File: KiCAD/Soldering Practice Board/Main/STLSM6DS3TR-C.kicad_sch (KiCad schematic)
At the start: 1 part, among them U3 LSM6DS3

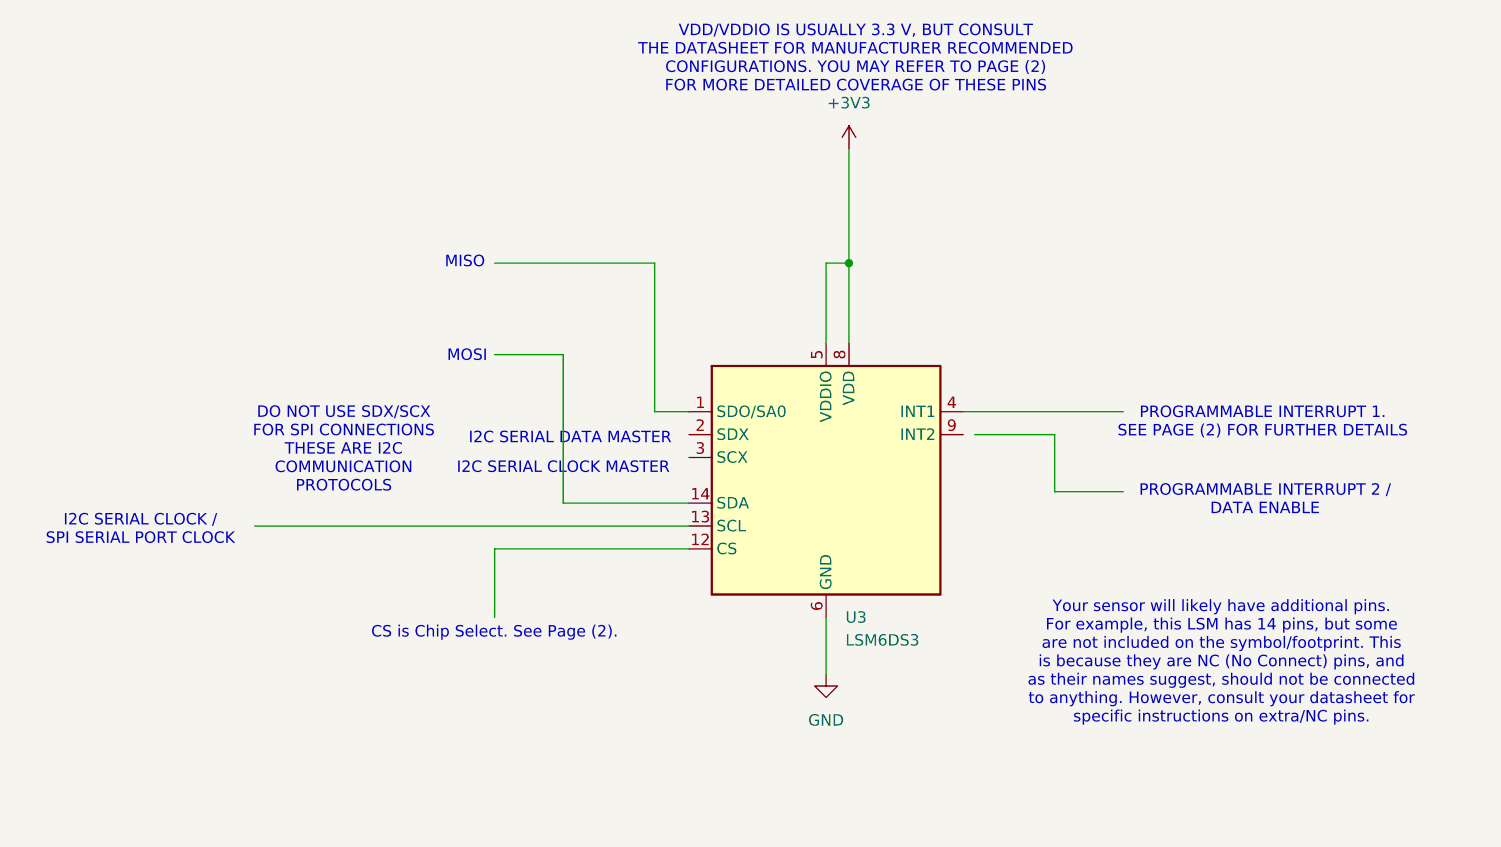
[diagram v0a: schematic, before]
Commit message: Make LIS3 labels more concise
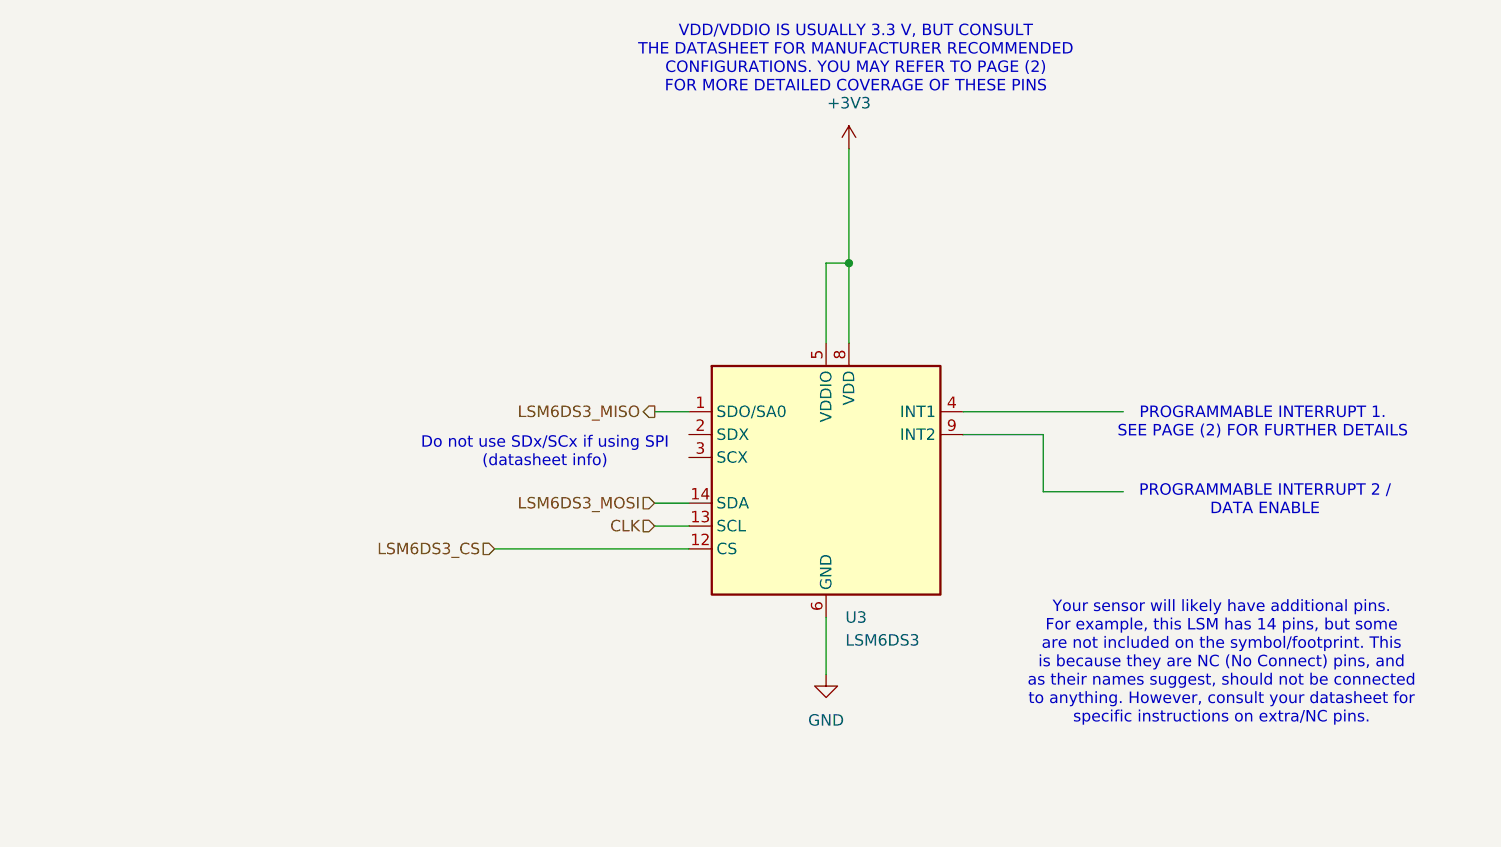
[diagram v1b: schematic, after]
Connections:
- net LSM6DS3_MISO: now reaches U3.1 (SDO/SA0)
- net LSM6DS3_CS: now reaches U3.12 (CS)
- net CLK: now reaches U3.13 (SCL)
- net LSM6DS3_MOSI: now reaches U3.14 (SDA)
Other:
- note added: "Do not use SDx/SCx if using SPI (datasheet info)"
- note removed: "CS is Chip Select. See Page (2)."
- note removed: "DO NOT USE SDX/SCX FOR SPI CONNECTIONS THESE ARE I2C COMMUNICATION PROTOCOLS"
- note removed: "I2C SERIAL CLOCK / SPI SERIAL PORT CLOCK"
- note removed: "I2C SERIAL CLOCK MASTER"
- note removed: "I2C SERIAL DATA MASTER"
- note removed: "MISO"
- note removed: "MOSI"
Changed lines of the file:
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@@
 	(generator_version "9.0")
 	(paper "A4")
-	(text "DO NOT USE SDX/SCX\nFOR SPI CONNECTIONS\nTHESE ARE I2C\nCOMMUNICATION\nPROTOCOLS"
-		(exclude_from_sim no)
-		(at 91.186 97.028 0)
+	(text "Do not use SDx/SCx if using SPI \n(datasheet info)"
+		(exclude_from_sim no)
+		(at 113.538 97.282 0)
 		(effects
 			(font
@@
 		)
 	)
-	(text "MOSI"
-		(exclude_from_sim no)
-		(at 104.902 86.614 0)
-		(effects
-			(font
-				(size 1.27 1.27)
-			)
-		)
-	)
-	(text "I2C SERIAL DATA MASTER"
-		(exclude_from_sim no)
-		(at 116.332 95.758 0)
-		(effects
-			(font
-				(size 1.27 1.27)
-			)
-		)
-	)
 	(text "VDD/VDDIO IS USUALLY 3.3 V, BUT CONSULT\nTHE DATASHEET FOR MANUFACTURER RECOMMENDED\nCONFIGURATIONS. YOU MAY REFER TO PAGE (2)\nFOR MORE DETAILED COVERAGE OF THESE PINS"
 		(exclude_from_sim no)
@@
 		)
 	)
-	(text "MISO"
-		(exclude_from_sim no)
-		(at 104.648 76.2 0)
-		(effects
-			(font
-				(size 1.27 1.27)
-			)
-		)
-	)
 	(text "Your sensor will likely have additional pins.\nFor example, this LSM has 14 pins, but some\nare not included on the symbol/footprint. This\nis because they are NC (No Connect) pins, and \nas their names suggest, should not be connected\nto anything. However, consult your datasheet for\nspecific instructions on extra/NC pins."
 		(exclude_from_sim no)
 		(at 188.722 120.65 0)
-		(effects
-			(font
-				(size 1.27 1.27)
-			)
-		)
-	)
-	(text "CS is Chip Select. See Page (2)."
-		(exclude_from_sim no)
-		(at 107.95 117.348 0)
-		(effects
-			(font
-				(size 1.27 1.27)
-			)
-		)
-	)
-	(text "I2C SERIAL CLOCK / \nSPI SERIAL PORT CLOCK"
-		(exclude_from_sim no)
-		(at 68.58 105.918 0)
-		(effects
-			(font
-				(size 1.27 1.27)
-			)
-		)
-	)
-	(text "I2C SERIAL CLOCK MASTER"
-		(exclude_from_sim no)
-		(at 115.57 99.06 0)
 		(effects
 			(font
@@
 	(wire
 		(pts
-			(xy 161.29 95.25) (xy 170.18 95.25)
+			(xy 160.02 95.25) (xy 168.91 95.25)
 		)
 		(stroke
@@
 	(wire
 		(pts
-			(xy 125.73 92.71) (xy 125.73 76.2)
-		)
-		(stroke
-			(width 0)
-			(type default)
-		)
-	)
-	(wire
-		(pts
-			(xy 115.57 102.87) (xy 129.54 102.87)
-		)
-		(stroke
-			(width 0)
-			(type default)
-		)
-	)
-	(wire
-		(pts
-			(xy 115.57 102.87) (xy 115.57 86.36)
+			(xy 125.73 102.87) (xy 129.54 102.87)
 		)
 		(stroke
@@
 	(wire
 		(pts
-			(xy 107.95 86.36) (xy 115.57 86.36)
-		)
-		(stroke
-			(width 0)
-			(type default)
-		)
-	)
-	(wire
-		(pts
-			(xy 107.95 107.95) (xy 107.95 115.57)
-		)
-		(stroke
-			(width 0)
-			(type default)
-		)
-	)
-	(wire
-		(pts
-			(xy 170.18 95.25) (xy 170.18 101.6)
+			(xy 168.91 95.25) (xy 168.91 101.6)
+		)
+		(stroke
+			(width 0)
+			(type default)
+		)
+	)
+	(wire
+		(pts
+			(xy 144.78 85.09) (xy 144.78 76.2)
+		)
+		(stroke
+			(width 0)
+			(type default)
+		)
+	)
+	(wire
+		(pts
+			(xy 125.73 105.41) (xy 129.54 105.41)
+		)
+		(stroke
+			(width 0)
+			(type default)
+		)
+	)
+	(wire
+		(pts
+			(xy 107.95 107.95) (xy 129.54 107.95)
 		)
 		(stroke
@@
 	(wire
 		(pts
-			(xy 144.78 85.09) (xy 144.78 76.2)
-		)
-		(stroke
-			(width 0)
-			(type default)
-		)
-	)
-	(wire
-		(pts
-			(xy 81.28 105.41) (xy 129.54 105.41)
-		)
-		(stroke
-			(width 0)
-			(type default)
-		)
-	)
-	(wire
-		(pts
-			(xy 107.95 107.95) (xy 129.54 107.95)
-		)
-		(stroke
-			(width 0)
-			(type default)
-		)
-	)
-	(wire
-		(pts
-			(xy 107.95 76.2) (xy 125.73 76.2)
-		)
-		(stroke
-			(width 0)
-			(type default)
-		)
-	)
-	(wire
-		(pts
 			(xy 160.02 92.71) (xy 177.8 92.71)
 		)
@@
 	(wire
 		(pts
-			(xy 170.18 101.6) (xy 177.8 101.6)
-		)
-		(stroke
-			(width 0)
-			(type default)
-		)
-	)
+			(xy 168.91 101.6) (xy 177.8 101.6)
+		)
+		(stroke
+			(width 0)
+			(type default)
+		)
+	)
+	(hierarchical_label "CLK"
+		(shape input)
+		(at 125.73 105.41 180)
+		(effects
+			(font
+				(size 1.27 1.27)
+			)
+			(justify right)
+		)
+	)
+	(hierarchical_label "LSM6DS3_MISO"
+		(shape output)
+		(at 125.73 92.71 180)
+		(effects
+			(font
+				(size 1.27 1.27)
+			)
+			(justify right)
+		)
+	)
+	(hierarchical_label "LSM6DS3_CS"
+		(shape input)
+		(at 107.95 107.95 180)
+		(effects
+			(font
+				(size 1.27 1.27)
+			)
+			(justify right)
+		)
+	)
+	(hierarchical_label "LSM6DS3_MOSI"
+		(shape input)
+		(at 125.73 102.87 180)
+		(effects
+			(font
+				(size 1.27 1.27)
+			)
+			(justify right)
+		)
+	)

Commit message: copy mode 1 schematic for lsm
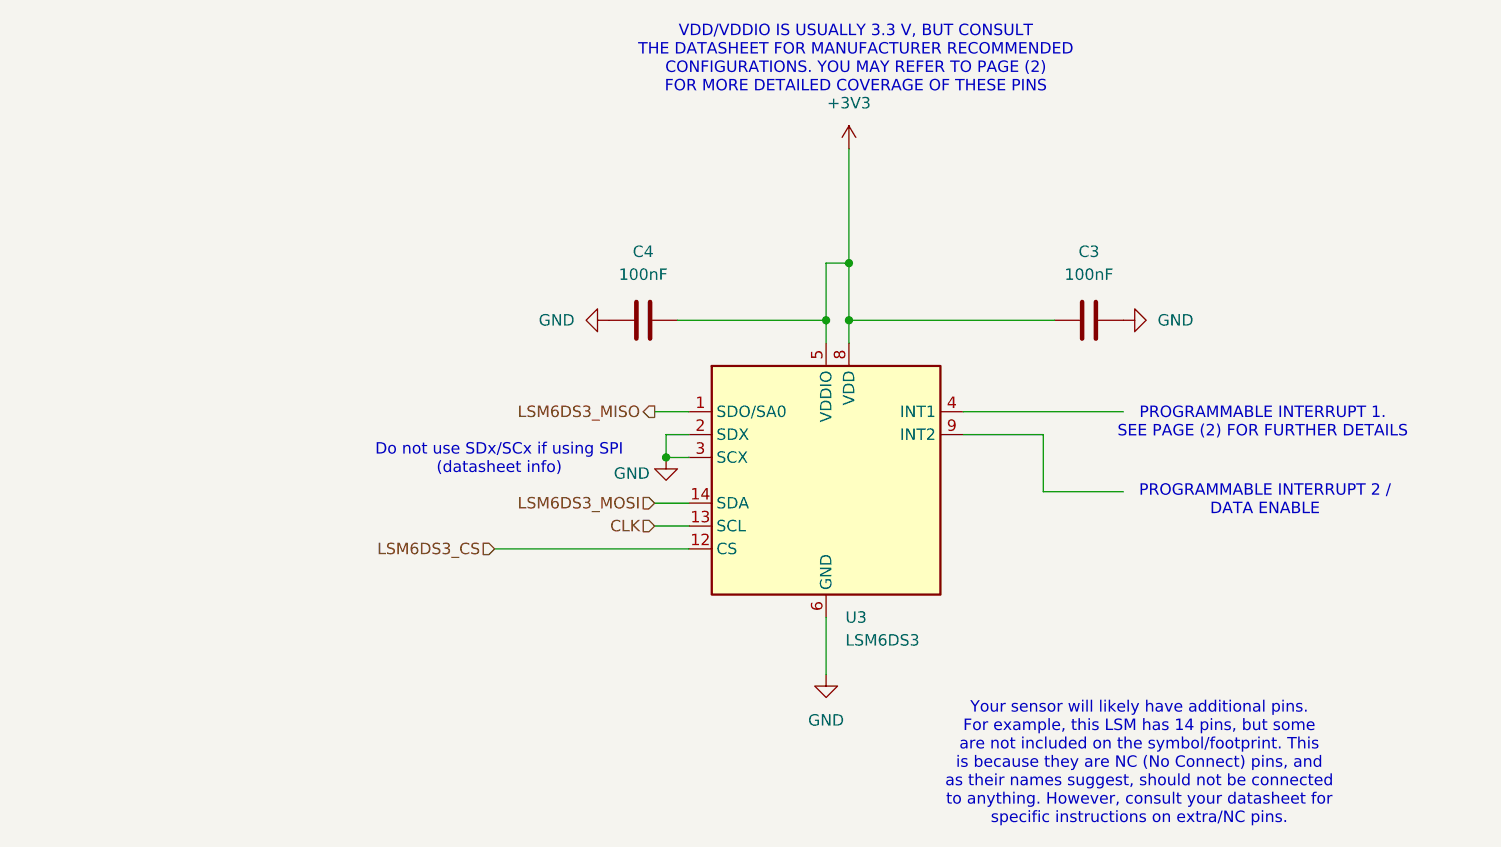
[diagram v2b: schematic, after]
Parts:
- added C3, C4: 100nF, symbol Device:C
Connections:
- net +3V3: now also C3.1, C4.2
- net GND: now also U3.2 (SDX), U3.3 (SCX), C3.2, C4.1

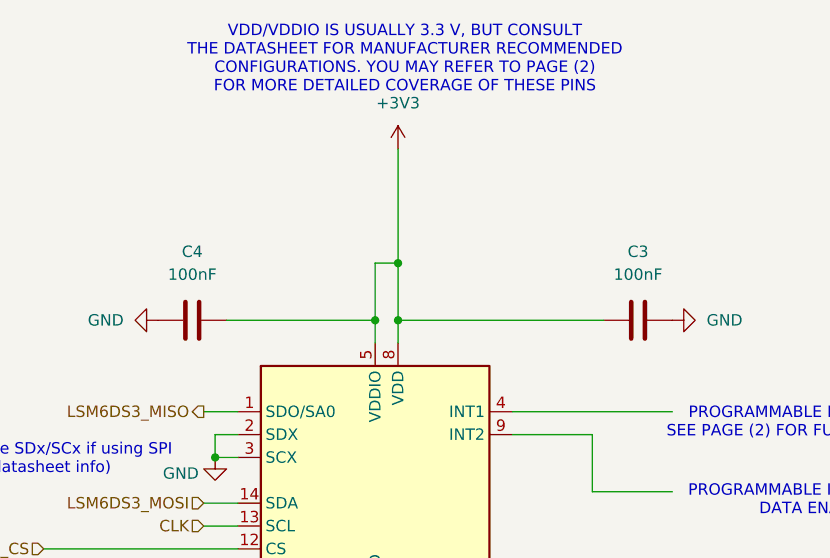
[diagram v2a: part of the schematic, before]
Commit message: Configure IOC file, rename pins
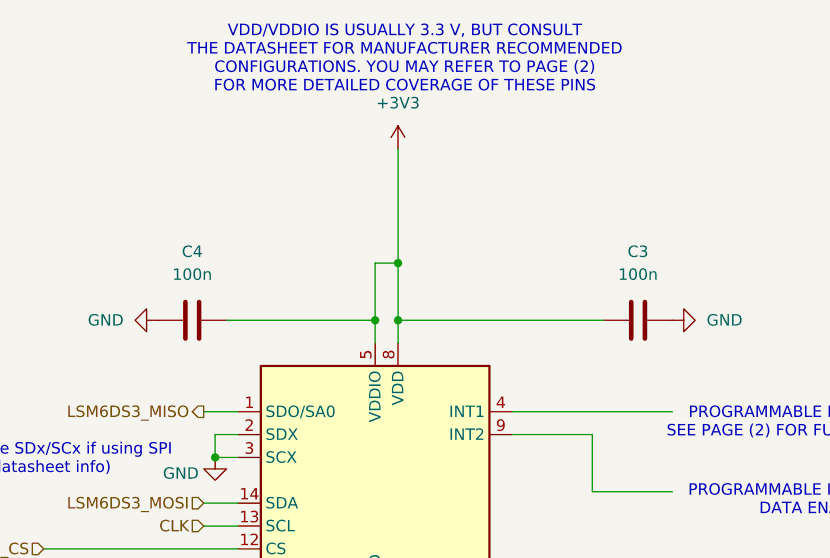
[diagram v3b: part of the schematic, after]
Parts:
- C3, C4: value 100nF -> 100n; footprint (none) -> Capacitor_SMD:C_0603_1608Metric
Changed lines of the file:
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@@
 			)
 		)
-		(property "Value" "100nF"
+		(property "Value" "100n"
 			(at 124.46 77.47 90)
 			(effects
@@
 			)
 		)
-		(property "Footprint" ""
+		(property "Footprint" "Capacitor_SMD:C_0603_1608Metric"
 			(at 128.27 81.5848 0)
 			(effects
@@
 			)
 		)
-		(property "Value" "100nF"
+		(property "Value" "100n"
 			(at 173.99 77.47 90)
 			(effects
@@
 			)
 		)
-		(property "Footprint" ""
+		(property "Footprint" "Capacitor_SMD:C_0603_1608Metric"
 			(at 177.8 81.5848 0)
 			(effects
